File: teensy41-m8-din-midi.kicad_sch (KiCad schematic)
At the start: 12 parts, among them J1 IN, J2 OUT, SW1 OUT_CONFIG, SW2 IN_CONFIG, U1 Teensy4.1, U2 6N138

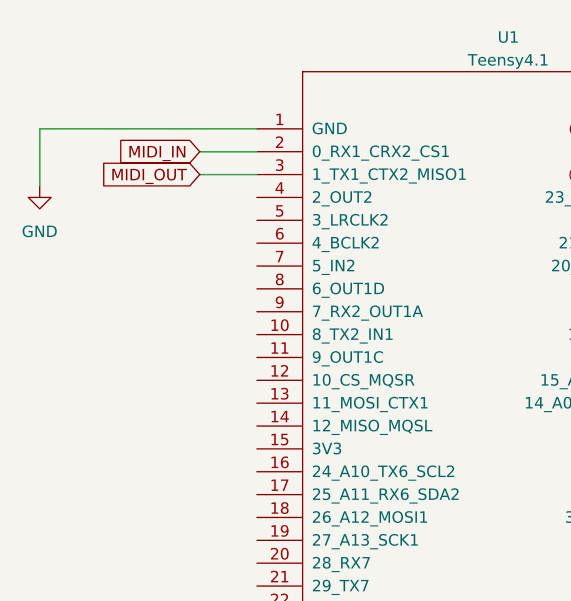
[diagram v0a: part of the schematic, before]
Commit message: Fixed pin assignments
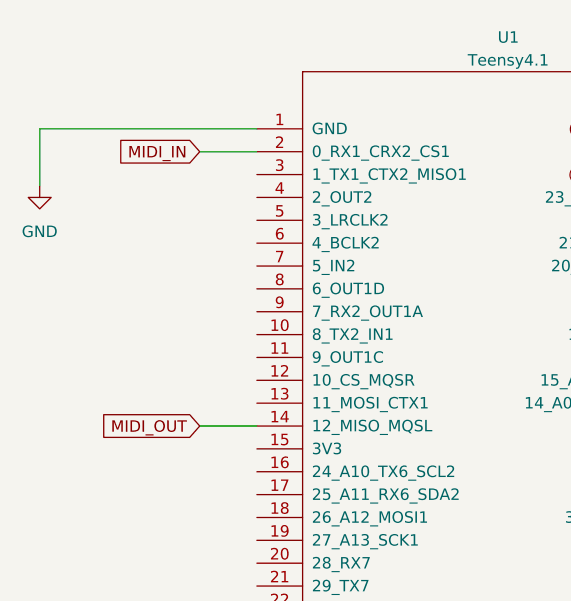
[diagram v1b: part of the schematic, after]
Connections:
- net MIDI_OUT: now also U1.14 (12_MISO_MQSL); no longer U1.3 (1_TX1_CTX2_MISO1)
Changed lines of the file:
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@@
-    (stroke (width 0) (type default))
-  )
-  (wire (pts (xy 57.15 52.07) (xy 63.5 52.07))
     (stroke (width 0) (type default))
   )
@@
   )
   (wire (pts (xy 190.5 73.66) (xy 190.5 67.31))
+    (stroke (width 0) (type default))
+  )
+  (wire (pts (xy 57.15 80.01) (xy 63.5 80.01))
     (stroke (width 0) (type default))
   )
@@
     )
   )
-  (global_label "MIDI_OUT" (shape input) (at 57.15 52.07 180) (fields_autoplaced)
+  (global_label "MIDI_OUT" (shape input) (at 57.15 80.01 180) (fields_autoplaced)
     (effects (font (size 1.27 1.27)) (justify right))
-    (property "Intersheetrefs" "${INTERSHEET_REFS}" (at 45.717 52.07 0)
+    (property "Intersheetrefs" "${INTERSHEET_REFS}" (at 45.717 80.01 0)
       (effects (font (size 1.27 1.27)) (justify right) hide)
     )
